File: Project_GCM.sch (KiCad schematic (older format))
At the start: 19 parts, among them J1 Conn_02x04_Odd_Even, J12 Conn_02x21_Odd_Even, J7 3-641124-6, U1 LM810, U11 74AHC1G04, U2 LTC6994-1, U3 74AHC1G32, U5 74AHC1G04

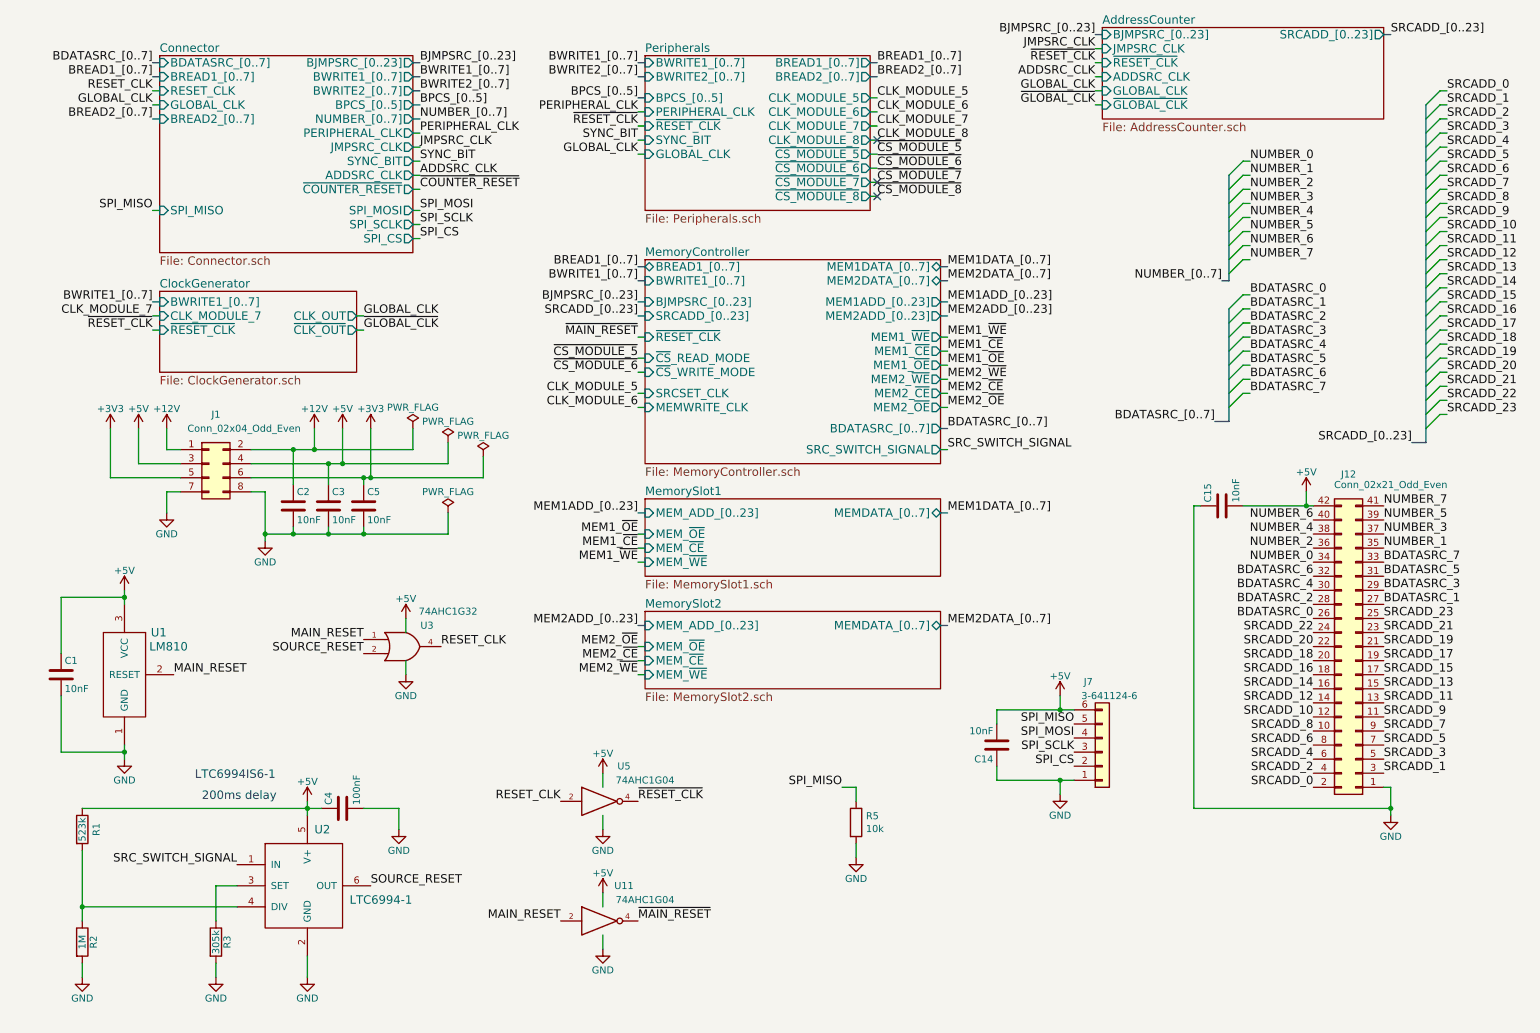
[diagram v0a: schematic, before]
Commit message: Adding copyright and license notice
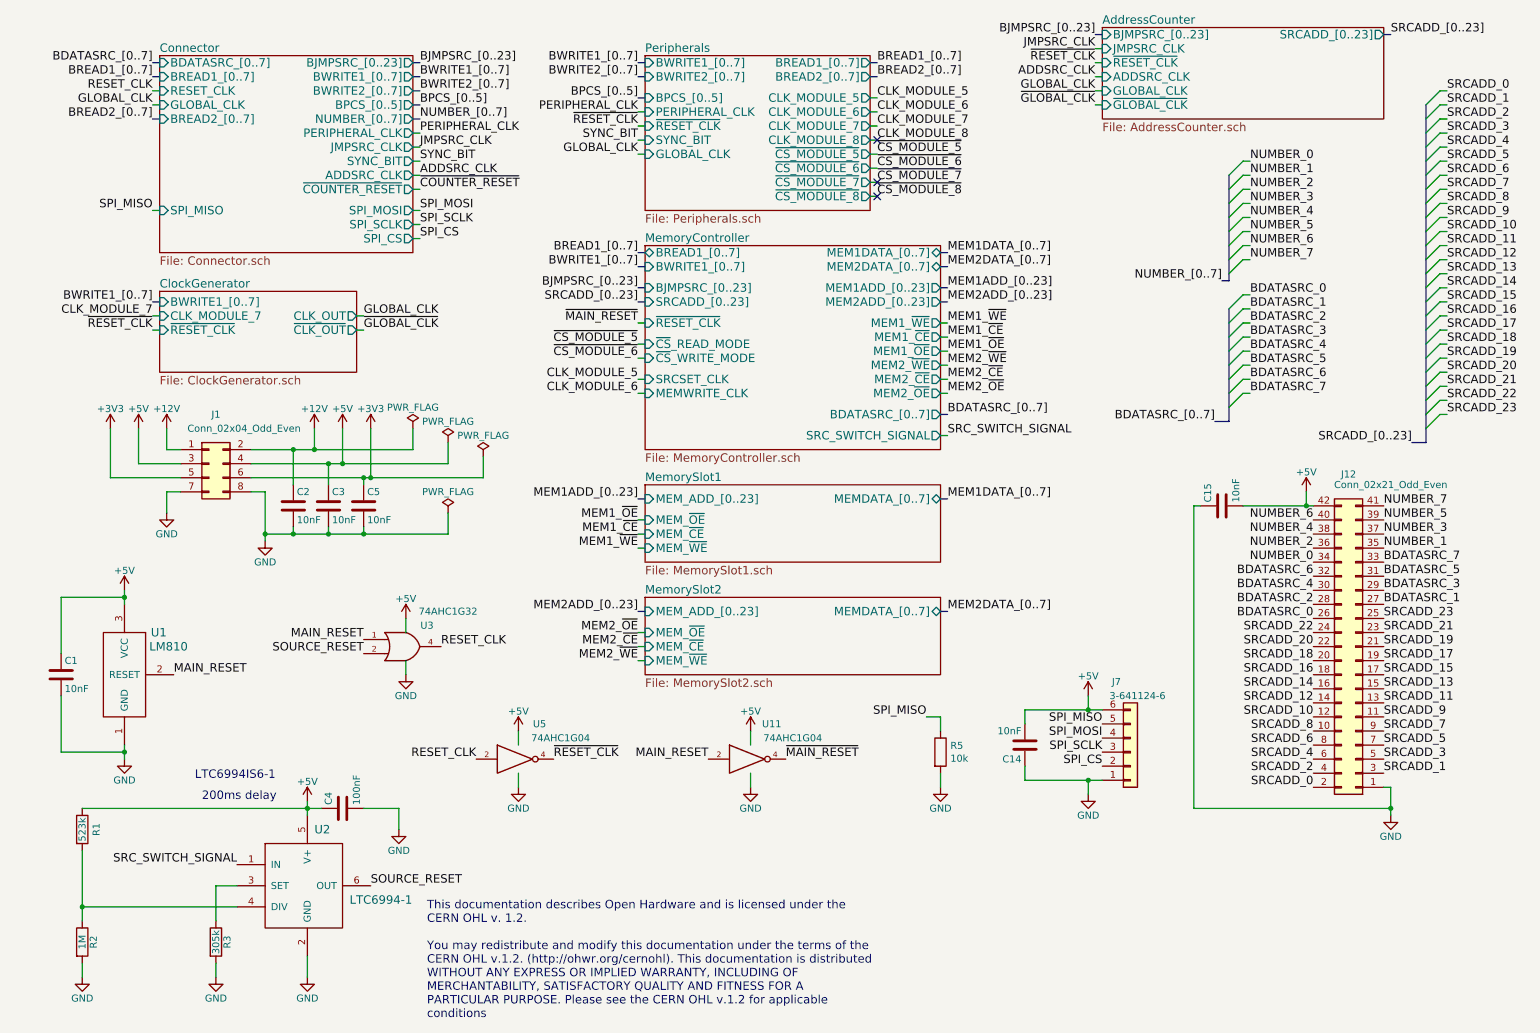
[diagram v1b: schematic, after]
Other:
- note added: "This documentation describes Open Hardware and is licensed under the\nCERN OHL v. 1.2.\n\nYou may redistribute and modify this documentation under the terms of the\nCERN OHL v.1.2. (http://ohwr.org/cernohl). This documentation is distributed\nWITHOUT ANY EXPRESS OR IMPLIED WARRANTY, INCLUDING OF\nMERCHANTABILITY, SATISFACTORY QUALITY AND FITNESS FOR A\nPARTICULAR PURPOSE. Please see the CERN OHL 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"
- moved on the sheet: C14, J7, R5, U11, U5

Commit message: Applying V5.0 and license to files
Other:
- note added: "This source describes Open Hardware and is licensed\nunder the CERN-OHL-W v2 or later. \n\nYou may redistribute and modify this documentation and make products\nusing it under the terms of the CERN-OHL-W v2 (https:/cern.ch/cern-ohl).\nThis documentation is distributed WITHOUT ANY EXPRESS OR IMPLIED WARRANTY,\nINCLUDING OF MERCHANTABILITY, SATISFACTORY QUALITY AND FITNESS FOR\nA PARTICULAR PURPOSE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"
- note removed: "This documentation describes Open Hardware and is licensed under the\nCERN OHL v. 1.2.\n\nYou may redistribute and modify this documentation under the terms of the\nCERN OHL v.1.2. (http://ohwr.org/cernohl). This documentation is distributed\nWITHOUT ANY EXPRESS OR IMPLIED WARRANTY, INCLUDING OF\nMERCHANTABILITY, SATISFACTORY QUALITY AND FITNESS FOR A\nPARTICULAR PURPOSE. Please see the CERN OHL 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"
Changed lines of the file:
@@
 EESchema Schematic File Version 4
-LIBS:Project_GCM-cache
 EELAYER 30 0
 EELAYER END
@@
 Title "GCM"
 Date "2019-07-07"
-Rev "V4"
+Rev "V5.0"
 Comp "Guillaume Guillet"
 Comment1 "Copyright Guillaume Guillet 2020"
-Comment2 "Licensed under CERN OHL v.1.2"
+Comment2 "Licensed under CERN-OHL-W v2 or later"
 Comment3 ""
 Comment4 ""
@@
 Text Label 1950 6650 2    60   ~ 0
 SRC_SWITCH_SIGNAL
-Text Notes 3300 7750 0    60   ~ 0
-This documentation describes Open Hardware and is licensed under the\nCERN OHL v. 1.2.\n\nYou may redistribute and modify this documentation under the terms of the\nCERN OHL v.1.2. (http://ohwr.org/cernohl). This documentation is distributed\nWITHOUT ANY EXPRESS OR IMPLIED WARRANTY, INCLUDING OF\nMERCHANTABILITY, SATISFACTORY QUALITY AND FITNESS FOR A\nPARTICULAR PURPOSE. Please see the CERN OHL v.1.2 for applicable\nconditions
+Text Notes 3250 7750 0    60   ~ 0
+This source describes Open Hardware and is licensed\nunder the CERN-OHL-W v2 or later. \n\nYou may redistribute and modify this documentation and make products\nusing it under the terms of the CERN-OHL-W v2 (https:/cern.ch/cern-ohl).\nThis documentation is distributed WITHOUT ANY EXPRESS OR IMPLIED WARRANTY,\nINCLUDING OF MERCHANTABILITY, SATISFACTORY QUALITY AND FITNESS FOR\nA PARTICULAR PURPOSE.\n\nPlease see the CERN-OHL-W v2 for applicable conditions.
 Wire Bus Line
 	9000 1750 9000 2500

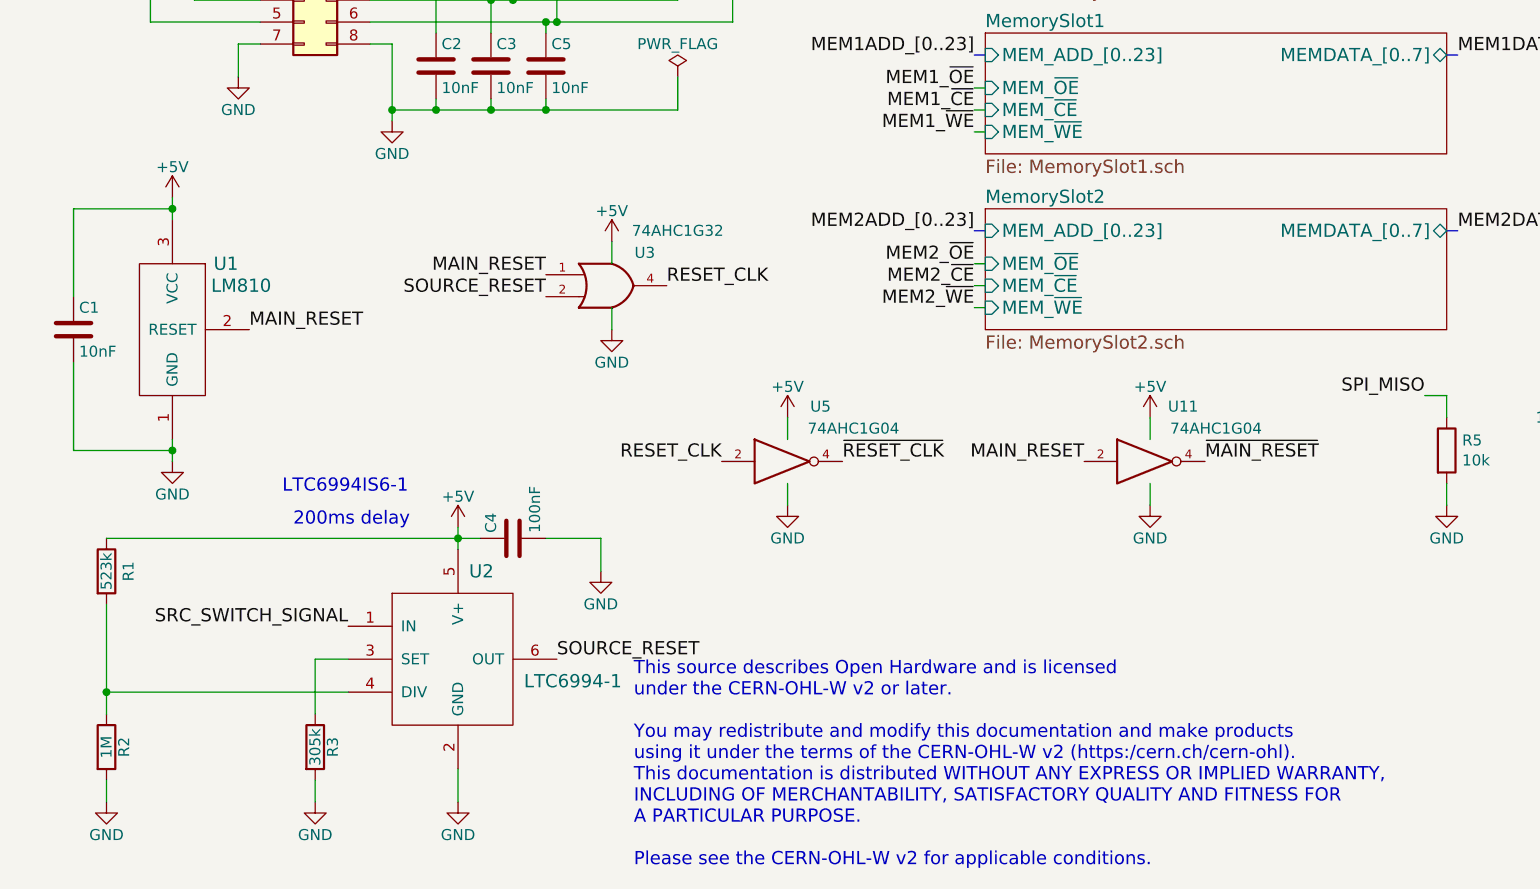
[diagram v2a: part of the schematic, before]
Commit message: Multiple change : Replacing old custom "LTC6994-1" symbol with the Kicad symbol "LTC6994xS6-1" Replacing old custom "LM810" symbol with the Kicad symbol "LM810" Replacing all hidden power pins symbols (hidden pins bug) Renaming "Main connector" to "SPS1 Processor connector" Removing old symbols, cleaning Replacing symbol "CD74AC238" with a new one
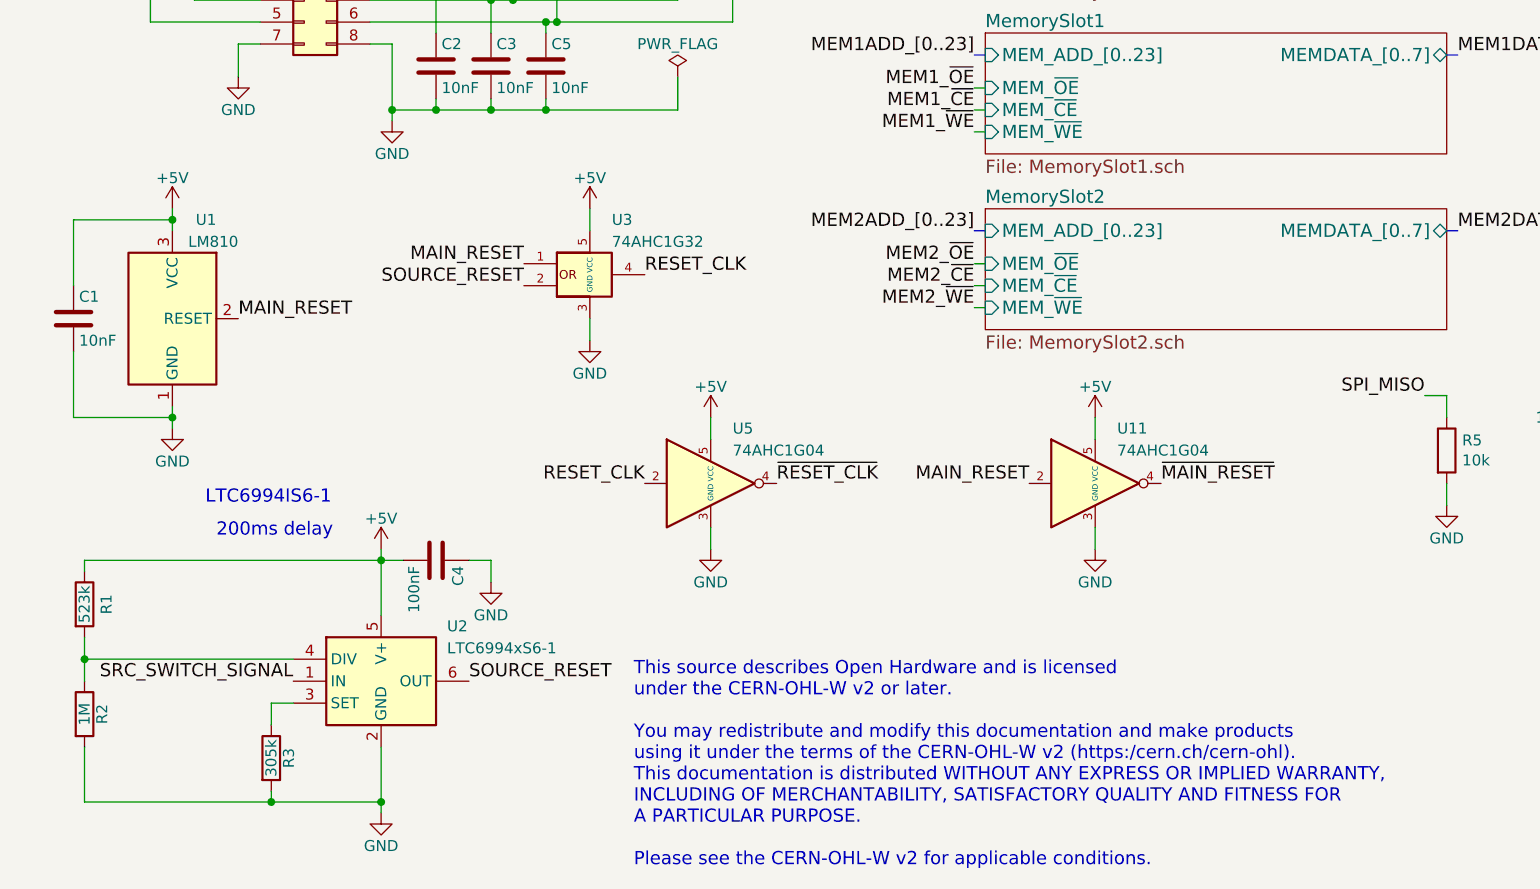
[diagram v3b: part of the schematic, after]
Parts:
- removed U1: LM810, Package_TO_SOT_SMD:SOT-23_Handsoldering, symbol Custom:LM810
- removed U11, U5: 74AHC1G04, Package_TO_SOT_SMD:SOT-23-5, symbol 74xGxx:74AHC1G04
- removed U2: LTC6994-1, Package_TO_SOT_SMD:SOT-23-6, symbol Custom:LTC6994-1
- removed U3: 74AHC1G32, Package_TO_SOT_SMD:SOT-23-5, symbol 74xGxx:74AHC1G32
- added U1: LM810, Package_TO_SOT_SMD:SOT-23, symbol Power_Supervisor:LM810
- added U11, U5: 74AHC1G04, symbol Custom:74AHC1G04
- added U2: LTC6994xS6-1, Package_TO_SOT_SMD:TSOT-23-6, symbol Timer:LTC6994xS6-1
- added U3: 74AHC1G32, symbol Custom:74AHC1G32
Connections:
- net +5V: now also C4.2, U1.3 (VCC), U11.5 (VCC), U2.5 (V+), U3.5 (VCC), U5.5 (VCC); no longer C4.1
- net GND: now also C4.1, U1.1 (GND), U11.3 (GND), U2.2 (GND), U3.3 (GND), U5.3 (GND); no longer C4.2
- net MAIN_RESET: now also U1.2 (RESET), U11.2, U3.1
- net RESET_CLK: now also U3.4, U5.2
- net SOURCE_RESET: now also U2.6 (OUT), U3.2
- net SRC_SWITCH_SIGNAL: now also U2.1 (IN)
- net ~MAIN_RESET: now also U11.4
- net ~RESET_CLK: now also U5.4
- net at R1.2, R2.1: now also U2.4 (DIV)
- net at R3.1: now also U2.3 (SET)
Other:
- moved on the sheet: C1, C4, R1, R2, R3

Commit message: see CHANGELOG
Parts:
- added U25: 74AHC1G32, symbol Custom:74AHC1G32
- J1: value Conn_02x04_Odd_Even -> Alimentation
- J12: value Conn_02x21_Odd_Even -> DEBUG_BUSES
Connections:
- net +5V: now also U25.5 (VCC)
- net GND: now also U25.3 (GND)
- net SRC_SWITCH_SIGNAL: now also U25.2; no longer U2.1 (IN)
- net MAIN_RESET renamed POWER_RESET
- net RESET_CLK renamed GLOBAL_RESET
- net SOURCE_RESET renamed LIGHT_RESET
- net ~MAIN_RESET renamed ~POWER_RESET
- net ~RESET_CLK renamed ~GLOBAL_RESET
- new net FREQUENCY_SWITCH_SIGNAL: U25.1
- new net LIGHT_RESET_IN: U2.1 (IN), U25.4
- no-connect marks 3 -> 4
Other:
- moved on the sheet: C1, U1, U11, U3, U5
